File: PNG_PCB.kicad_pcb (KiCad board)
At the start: 2 copper layers, 128.5 x 111 mm, 139 parts, among them J1 solder pad, J10 solder pad, J11 solder pad, J12 solder pad, J13 solder pad, J14 solder pad, J15 solder pad, J16 solder pad, J17 solder pad, J18 solder pad, J19 solder pad, J2 solder pad, J20 solder pad, J21 solder pad, J22 solder pad, J23 solder pad, J24 solder pad, J25 solder pad, J26 solder pad, J27 solder pad, J28 solder pad, J29 solder pad, J3 solder pad, J30 solder pad, J31 solder pad, J32 solder pad, J33 solder pad, J34 solder pad, J35 solder pad, J36 solder pad, J37 solder pad, J38 solder pad, J39 solder pad, J4 solder pad, J40 solder pad, J41 solder pad, J42 solder pad, J43 solder pad, J44 solder pad, J45 solder pad, J46 solder pad, J47 solder pad, J48 solder pad, J49 solder pad, J5 solder pad, J50 solder pad, J51 solder pad, J52 solder pad, J53 solder pad, J54 solder pad, J55 solder pad, J56 solder pad, J57 solder pad, J58 solder pad, J59 solder pad, J6 solder pad, J60 solder pad, J7 solder pad, J8 solder pad, J9 solder pad, U1 Teensy4.1, U2 Mux, U3 MCP6004, U4 Mux, U5 Mux, U6 MCP6004, U7 Mux, U8 Mux, U9 MCP6004

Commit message: finished all amps
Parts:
- moved R59 49.5 mm to (180.2, 49.8)
- moved R66 49.1 mm to (180.2, 53.1)
- moved R16 41.5 mm to (159.5, 103.1)
- moved R20 39.4 mm to (165.0, 109.9)
- moved R19 39.2 mm to (159.5, 109.9)
- moved R18 39.1 mm to (165.0, 106.4)
- moved R15 38.9 mm to (159.5, 106.4)
- moved R21 38.7 mm to (165.0, 103.1)
- moved R26 35.0 mm to (175.3, 109.9)
- moved R27 34.9 mm to (170.1, 109.9)
- moved R22 34.6 mm to (175.3, 106.4)
- moved R25 34.5 mm to (170.1, 106.4)
- moved R28 34.0 mm to (170.1, 103.1)
- moved R1 33.6 mm to (175.3, 90.2)
- moved R11 33.6 mm to (165.0, 90.2)
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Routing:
- net /ampD0/V1: track 62.0 -> 8.54 mm, vias 0 -> 2
- net /ampC0/V1: track 69.4 -> 20.4 mm, vias 0 -> 2
- net /ampA0/mux0: track 41.2 -> 0.00 mm
- net /ampA0/mux1: track 32.8 -> 0.00 mm
- net GND: track 50.4 -> 82.8 mm, vias 9 -> 12
- net /ampB0/mux1: track 32.3 -> 0.00 mm
- net /ampA0/mux2: track 25.4 -> 0.00 mm
- net /ampB0/mux2: track 22.1 -> 0.00 mm
- net /ampB2/V1: track 0.00 -> 21.4 mm, vias 0 -> 2
- net /ampB0/V1: track 0.00 -> 20.3 mm, vias 0 -> 2
- net /ampA2/V1: track 0.00 -> 10.0 mm, vias 0 -> 2
- net /ampA0/V1: track 0.00 -> 8.54 mm, vias 0 -> 2
- net Net-(R26-Pad1): track 17.3 -> 12.8 mm
- net Net-(R19-Pad1): track 17.6 -> 13.1 mm
- net /ADC_IN_3: track 0.00 -> 2.57 mm
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
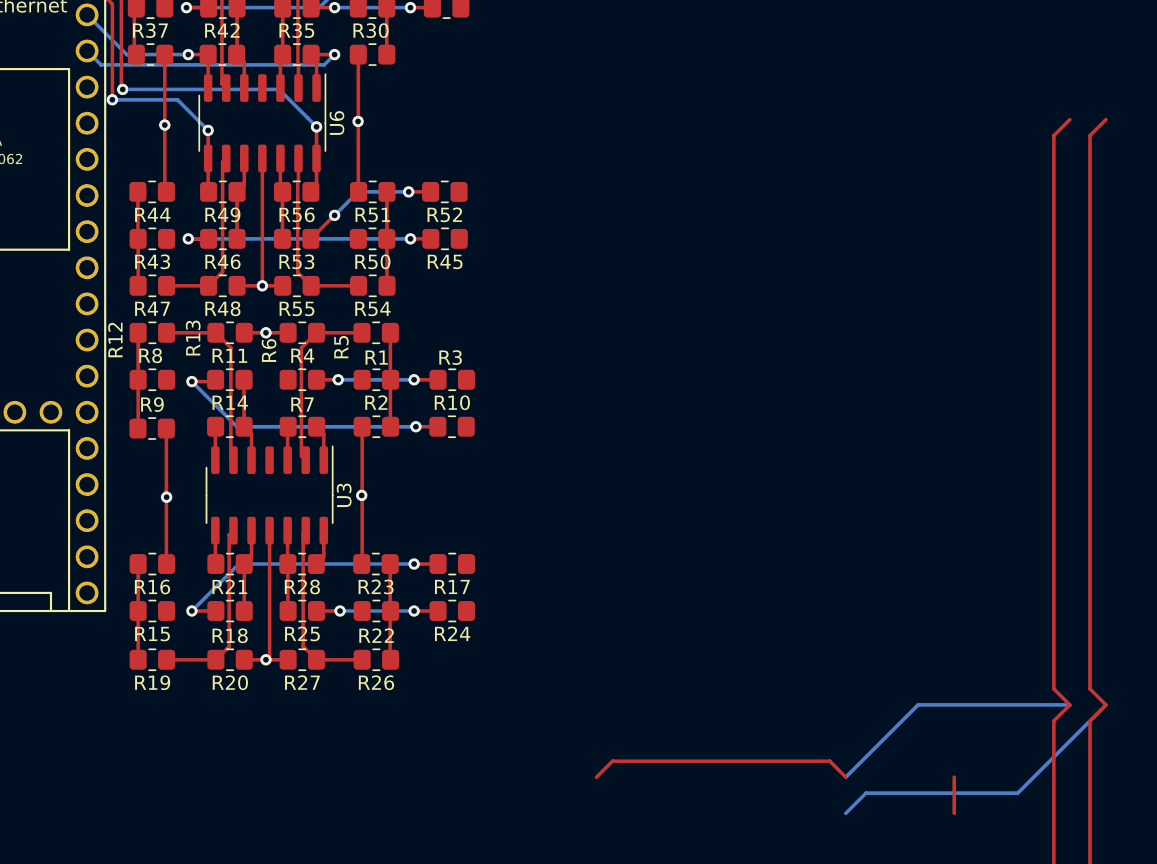
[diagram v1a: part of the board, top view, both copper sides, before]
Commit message: connected up all amps
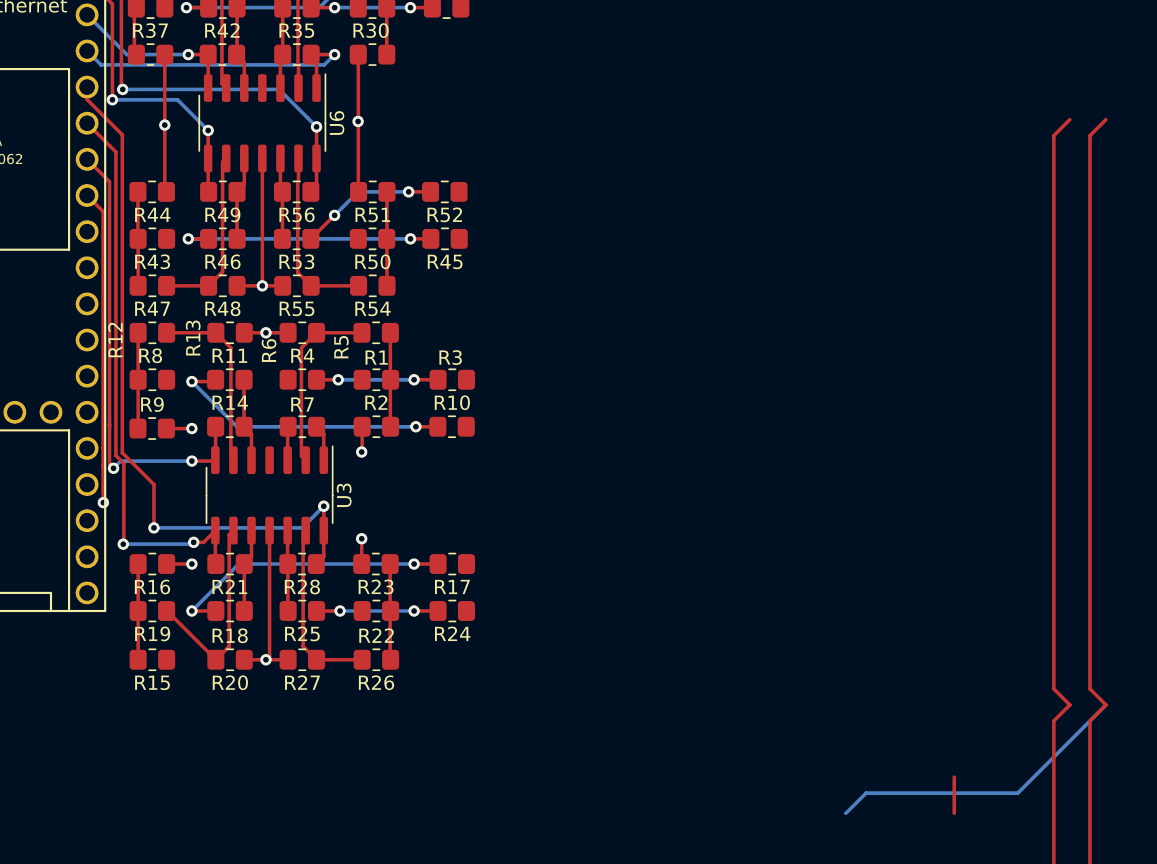
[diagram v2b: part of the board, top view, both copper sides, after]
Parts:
- moved R15 3.43 mm to (159.5, 109.9)
- moved R19 3.43 mm to (159.5, 106.4)
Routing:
- net /ADC_IN_3: track 2.57 -> 49.8 mm, vias 0 -> 2
- net /ADC_IN_2: track 2.36 -> 39.9 mm, vias 0 -> 2
- net /selB: track 104.7 -> 68.4 mm
- net /ADC_IN_1: track 2.36 -> 32.4 mm, vias 0 -> 2
- net /ADC_IN_0: track 2.56 -> 24.7 mm, vias 0 -> 1
- net GND: track 82.8 -> 70.0 mm, vias 12 -> 14
- net Net-(R19-Pad1): track 13.1 -> 14.5 mm

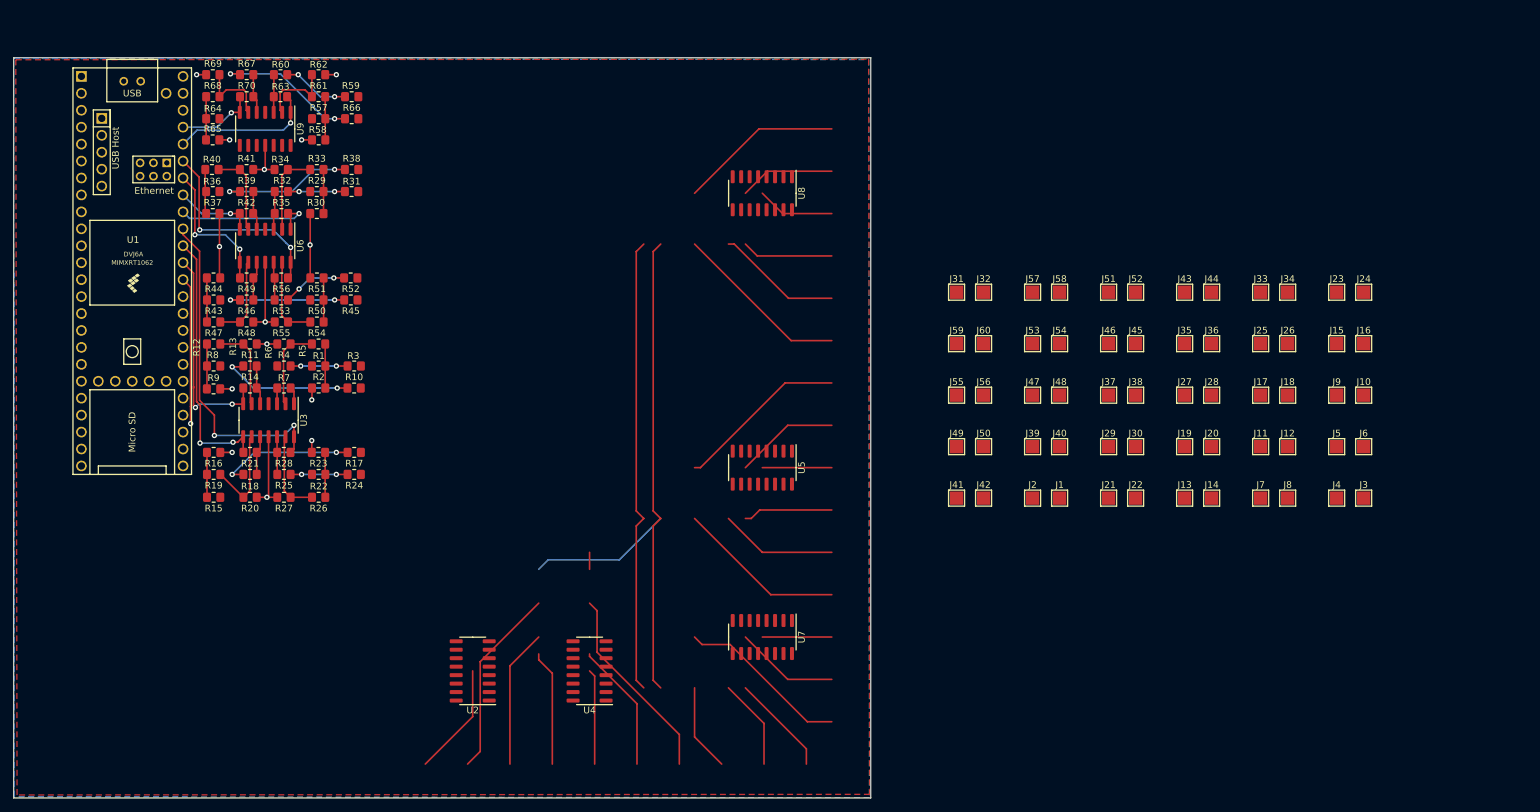
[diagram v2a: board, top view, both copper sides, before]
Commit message: reverted back to screw terminals
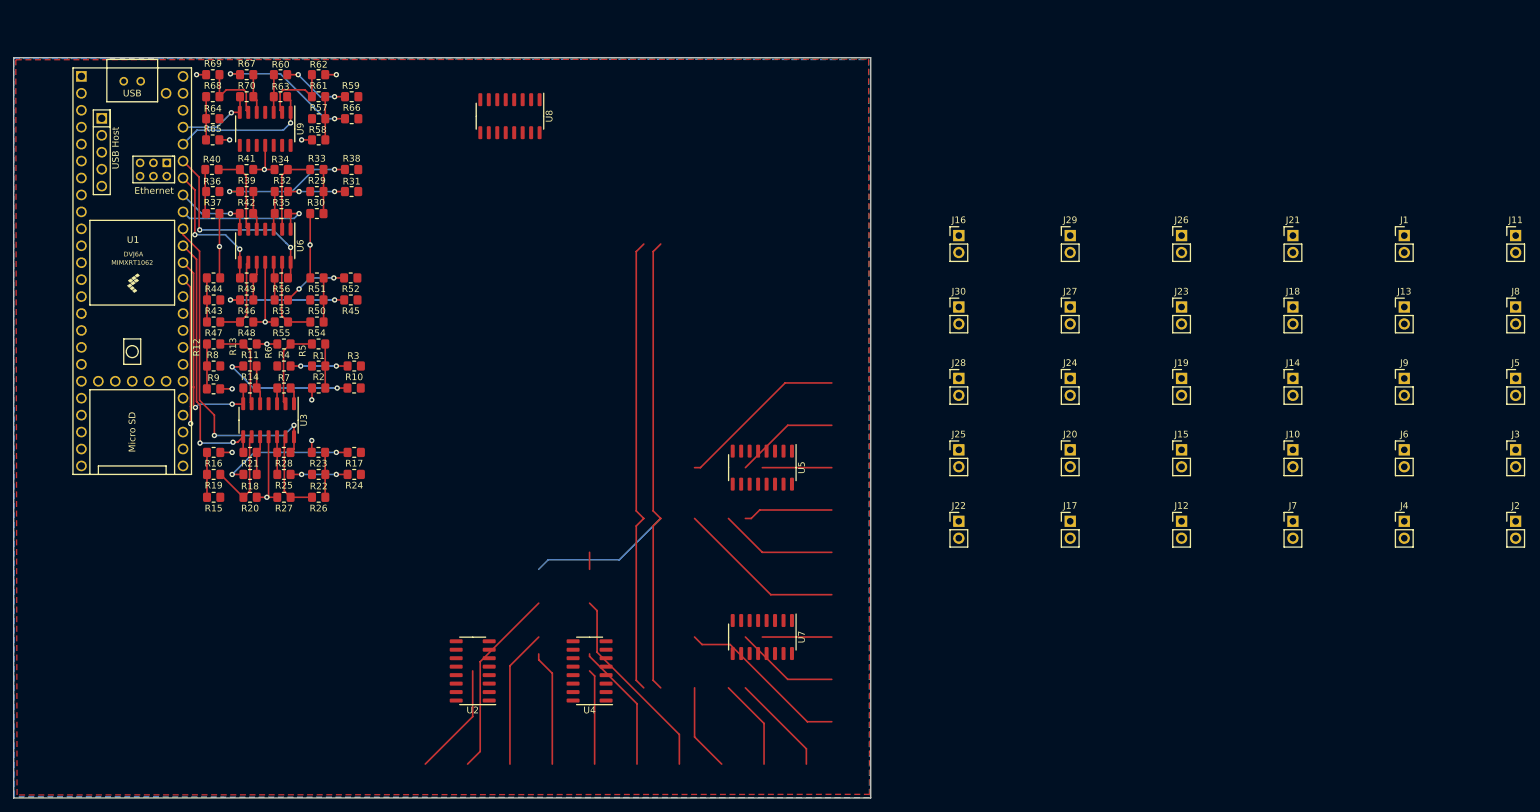
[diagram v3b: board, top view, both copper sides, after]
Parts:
- removed J31, J32, J33, J34, J35, J36, J37, J38, J39, J40, J41, J42, J43, J44, J45, J46, J47, J48, J49, J50, J51, J52, J53, J54, J55, J56, J57, J58, J59, J60: solder pad, TestPoint:TestPoint_Pad_2.0x2.0mm
- J1, J10, J11, J12, J13, J14, J15, J16, J17, J18, J19, J2, J20, J21, J22, J23, J24, J25, J26, J27, J28, J29, J3, J30, J4, J5, J6, J7, J8, J9: value solder pad -> screw terminal; footprint TestPoint:TestPoint_Pad_2.0x2.0mm -> Connector_PinHeader_2.54mm:PinHeader_1x02_P2.54mm_Vertical
- moved J2 72.5 mm to (354.8, 113.5)
- moved J1 65.0 mm to (338.1, 70.6)
- moved J16 62.8 mm to (271.3, 70.6)
- moved J11 49.6 mm to (354.8, 70.6)
- moved J21 48.1 mm to (321.4, 70.6)
- moved J25 48.0 mm to (271.3, 102.7)
- moved J24 45.9 mm to (288.0, 92.0)
- moved J8 44.6 mm to (354.8, 81.3)
- moved J13 43.7 mm to (338.1, 81.3)
- moved U8 39.6 mm to (204.0, 52.7)
- moved J28 38.0 mm to (271.3, 92.0)
- moved J17 34.3 mm to (288.0, 113.5)
- moved J30 33.8 mm to (271.3, 81.3)
- moved J29 32.2 mm to (288.0, 70.6)
- moved J5 28.7 mm to (354.8, 92.0)
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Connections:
- J1 pad 1: /ampA0/mux0 -> GND
- J11 pad 1: /ampB0/mux2 -> GND
- J13 pad 1: /ampC0/mux0 -> GND
- J15 pad 1: /ampC0/mux1 -> GND
- J17 pad 1: /ampC0/mux2 -> GND
- J19 pad 1: /ampD0/mux0 -> GND
- J21 pad 1: /ampD0/mux1 -> GND
- J23 pad 1: /ampD0/mux2 -> GND
- J25 pad 1: /ampA1/mux0 -> GND
- J27 pad 1: /ampA1/mux1 -> GND
- J29 pad 1: /ampA1/mux2 -> GND
- J3 pad 1: /ampA0/mux1 -> GND
- J5 pad 1: /ampA0/mux2 -> GND
- J7 pad 1: /ampB0/mux0 -> GND
- J9 pad 1: /ampB0/mux1 -> GND
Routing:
- net /ampA2/mux0: track 26.6 -> 0.00 mm
- net /ampA2/mux2: track 25.4 -> 0.00 mm
- net /ampB2/mux1: track 24.6 -> 0.00 mm
- net /ampA2/mux1: track 18.9 -> 0.00 mm
- net Net-(U8-Pad4): track 14.3 -> 0.00 mm

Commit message: changed to 1.00mm screw term holes
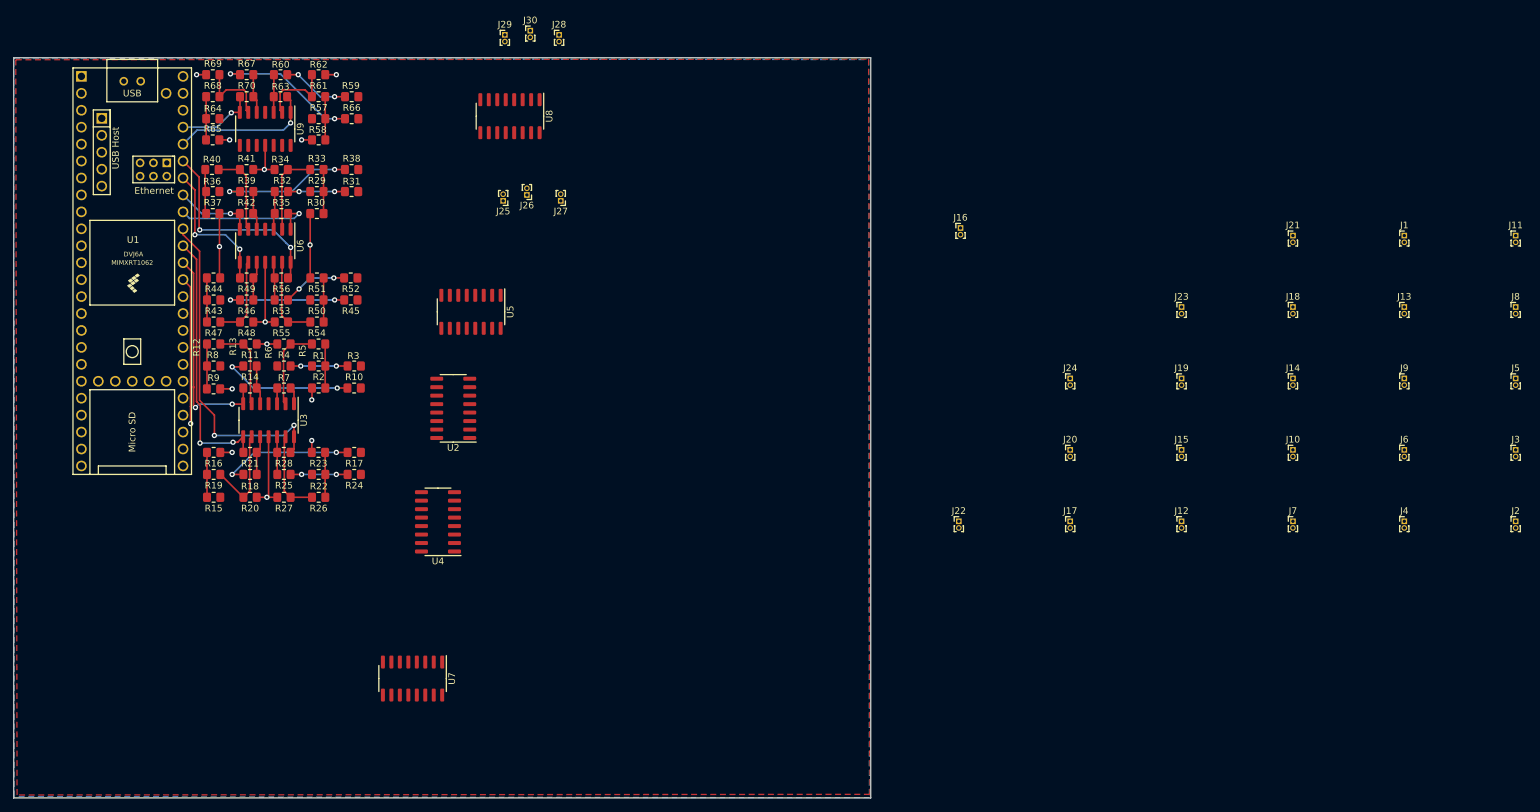
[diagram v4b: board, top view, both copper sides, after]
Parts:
- J1, J10, J11, J12, J13, J14, J15, J16, J17, J18, J19, J2, J20, J21, J22, J23, J24, J25, J26, J27, J28, J29, J3, J30, J4, J5, J6, J7, J8, J9: footprint Connector_PinHeader_2.54mm:PinHeader_1x02_P2.54mm_Vertical -> Connector_PinHeader_1.00mm:PinHeader_1x02_P1.00mm_Vertical
- moved J26 98.4 mm to (206.5, 64.5), turned to 180 degrees
- moved J29 90.0 mm to (203.2, 40.5)
- moved J28 79.0 mm to (211.3, 40.5)
- moved J27 78.0 mm to (211.6, 65.4), turned to 180 degrees
- moved J25 77.9 mm to (202.9, 65.4), turned to 180 degrees
- moved J30 76.5 mm to (207.0, 39.9)
- moved U7 52.8 mm to (189.4, 137.0)
- moved U5 49.5 mm to (198.1, 82.0)
- moved U2 39.5 mm to (195.5, 96.5)
- moved U4 31.9 mm to (193.2, 113.5)
- moved J16 1.17 mm to (271.5, 69.5)
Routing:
- net /selA: track 89.9 -> 0.00 mm
- net /selB: track 68.4 -> 0.00 mm
- net /ampD0/mux1: track 29.7 -> 0.00 mm
- net /ampC0/mux0: track 28.5 -> 0.00 mm
- net /ampB1/mux1: track 25.8 -> 0.00 mm
- net /ampD1/mux1: track 25.8 -> 0.00 mm
- net /ampA1/mux0: track 25.3 -> 0.00 mm
- net /ampC0/mux1: track 20.8 -> 0.00 mm
- net /ampD0/mux2: track 19.5 -> 0.00 mm
- net /ampA1/mux1: track 17.6 -> 0.00 mm
- net /ampC0/mux2: track 17.4 -> 0.00 mm
- net /ampB0/mux0: track 16.9 -> 0.00 mm
- net /ampD1/mux2: track 15.6 -> 0.00 mm
- net /ampB1/mux2: track 15.6 -> 0.00 mm
- net /ampC1/mux2: track 15.2 -> 0.00 mm
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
